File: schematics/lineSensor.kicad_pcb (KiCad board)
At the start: 2 copper layers, 27 parts, among them P1 CONN_01X01, P2 CONN_01X01, P3 CONN_01X01, P4 CONN_01X01, P5 CONN_01X01, P6 CONN_01X01, P7 CONN_01X01

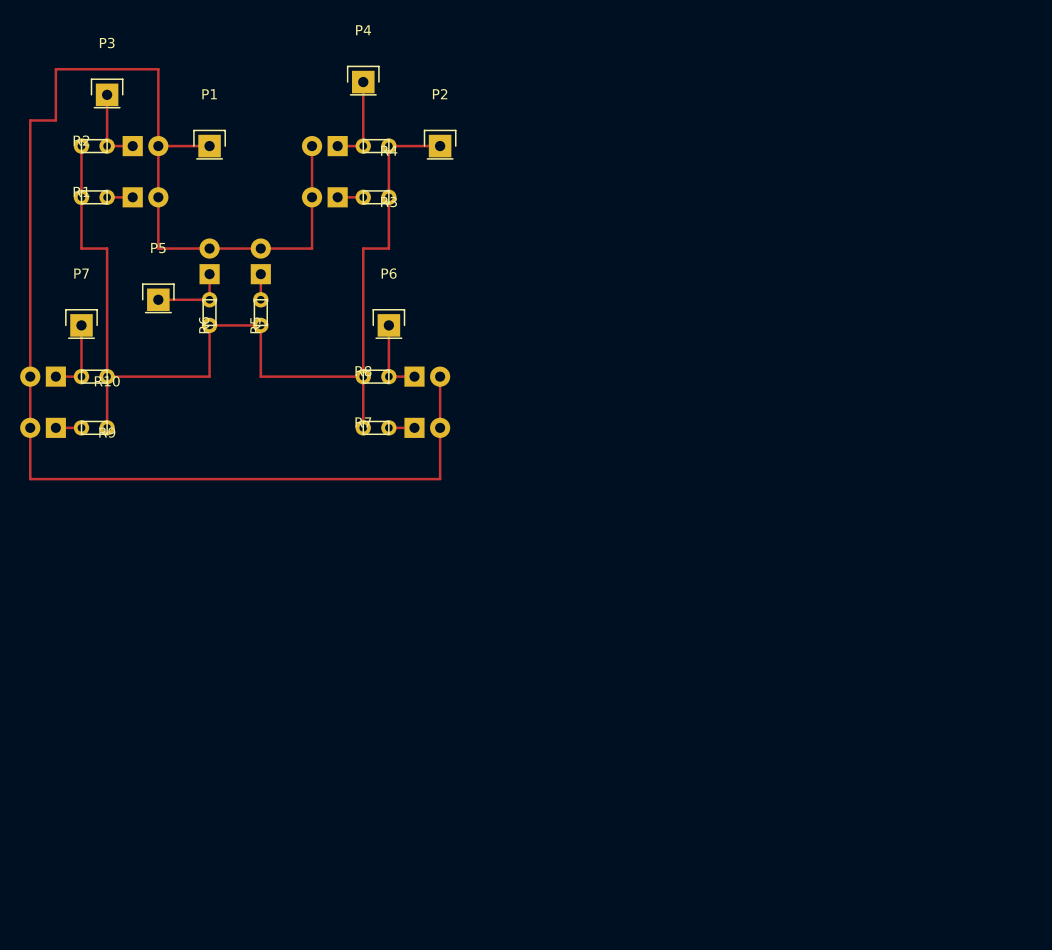
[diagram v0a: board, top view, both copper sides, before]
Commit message: Update LineSensor schematic
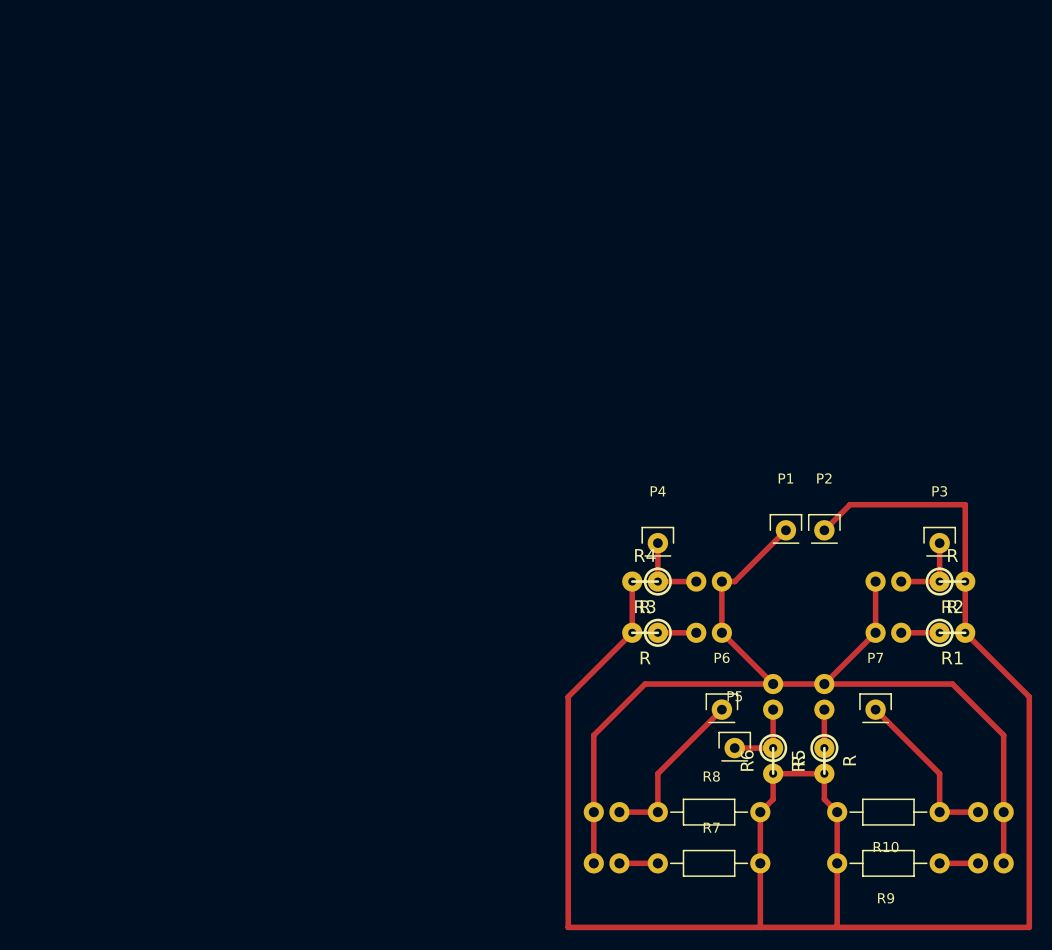
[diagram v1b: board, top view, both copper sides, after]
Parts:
- R1, R2, R3, R4, R5, R6: footprint MY:resistor2pins -> w_pth_resistors:rc05_vert
- R10, R7, R8, R9: footprint MY:resistor2pins -> Resistors_ThroughHole:Resistor_Horizontal_RM10mm
- moved D10 101.1 mm to (175.3, 121.9), turned to 0 degrees
- moved D9 101.1 mm to (175.3, 127.0), turned to 0 degrees
- moved R1 96.6 mm to (172.7, 104.1), turned to 0 degrees
- moved R2 96.6 mm to (172.7, 99.1), turned to 0 degrees
- moved P3 93.8 mm to (171.4, 95.2)
- moved R10 93.2 mm to (171.4, 121.9), turned to 180 degrees
- moved R9 93.2 mm to (171.4, 127.0), turned to 180 degrees
- moved D1 87.6 mm to (167.6, 104.1), turned to 180 degrees
- moved D2 87.6 mm to (167.6, 99.1), turned to 180 degrees
- moved P7 87.5 mm to (165.1, 111.8)
- moved P5 72.4 mm to (151.1, 115.6)
- moved D5 70.6 mm to (160.0, 111.8)
- moved R5 70.6 mm to (160.0, 116.8)
- moved D6 70.6 mm to (154.9, 111.8)
- moved R6 70.6 mm to (154.9, 116.8)
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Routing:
- net Net-(P2-Pad1): track 101.6 -> 178.8 mm
- net Net-(D1-Pad2): track 152.4 -> 103.2 mm
- net Net-(D8-Pad1): track 7.62 -> 16.6 mm
- net Net-(D10-Pad1): track 7.62 -> 16.6 mm
- net Net-(D7-Pad1): track 2.54 -> 3.81 mm
- net Net-(D3-Pad1): track 2.54 -> 3.81 mm
- net Net-(D1-Pad1): track 2.54 -> 3.81 mm
- net Net-(D9-Pad1): track 2.54 -> 3.81 mm
- net Net-(D4-Pad1): track 8.89 -> 7.62 mm
- net Net-(D5-Pad1): track 2.54 -> 3.81 mm
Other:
- rule pad_to_mask_clearance: 0.2 -> 0
